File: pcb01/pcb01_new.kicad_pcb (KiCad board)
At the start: 2 copper layers, 116.8 x 91.4 mm, 51 parts, among them J1 DIN41612_02x32_AC, J10 Conn_01x02_Socket, J11 Conn_01x09, J5 UART, J7 Jmp_Irq, J8 Jmp_NMI, J9 Ram1 Enable, SW1 SW_Push, U1 W65C02SxP, U10 TL28L92FR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

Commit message: more routing
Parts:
- added J2: Jmp_UART_Irq, Connector_PinSocket_2.54mm:PinSocket_1x02_P2.54mm_Vertical, F.Cu at (137.2, 36.8)
- added J3: Conn_01x09_Socket, Connector_PinHeader_2.54mm:PinHeader_1x09_P2.54mm_Vertical, F.Cu at (135.9, 29.8)
- added J4: Conn_01x08_Socket, Connector_PinSocket_2.54mm:PinSocket_1x08_P2.54mm_Vertical, F.Cu at (135.9, 24.8)
- moved J5 1.27 mm to (137.2, 58.4)
- moved C1 0.67 mm to (123.3, 34.9)
- moved Y1 0.62 mm to (119.4, 39.4)
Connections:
- U10 pad 10: unconnected-(U10-OP7-Pad10) -> /UART_OP7
- U10 pad 18: unconnected-(U10-INTRN-Pad18) -> /~{IRQ_UART}
- U10 pad 2: unconnected-(U10-IP0-Pad2) -> /UART_IP0
- U10 pad 24: unconnected-(U10-OP6-Pad24) -> /UART_OP6
- U10 pad 25: unconnected-(U10-OP4-Pad25) -> /UART_OP4
- U10 pad 26: unconnected-(U10-OP2-Pad26) -> /UART_OP2
- U10 pad 27: unconnected-(U10-OP0-Pad27) -> /UART_OP0
- U10 pad 34: unconnected-(U10-IP2-Pad34) -> /UART_IP2
- U10 pad 35: unconnected-(U10-IP6-Pad35) -> /UART_IP6
- U10 pad 36: unconnected-(U10-IP5-Pad36) -> /UART_IP5
- U10 pad 37: unconnected-(U10-IP4-Pad37) -> /UART_IP4
- U10 pad 41: unconnected-(U10-IP3-Pad41) -> /UART_IP3
- U10 pad 43: unconnected-(U10-IP1-Pad43) -> /UART_IP1
- U10 pad 7: unconnected-(U10-OP1-Pad7) -> /UART_OP1
- U10 pad 8: unconnected-(U10-OP3-Pad8) -> /UART_OP3
- U10 pad 9: unconnected-(U10-OP5-Pad9) -> /UART_OP5
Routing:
- net GND: track 420.1 -> 570.4 mm, vias 32 -> 31
- net /UART_IP6: track 0.00 -> 57.8 mm
- net /UART_OP4: track 0.00 -> 52.7 mm
- net /UART_IP2: track 0.00 -> 52.0 mm, vias 0 -> 1
- net /UART_OP0: track 0.00 -> 46.9 mm, vias 0 -> 1
- net /UART_OP6: track 0.00 -> 44.2 mm
- net /UART_IP5: track 0.00 -> 43.4 mm
- net /UART_OP2: track 0.00 -> 40.8 mm, vias 0 -> 1
- net /UART_IP4: track 0.00 -> 39.5 mm, vias 0 -> 1
- net /UART_IP3: track 0.00 -> 33.2 mm, vias 0 -> 1
- net /UART_IP1: track 0.00 -> 27.6 mm, vias 0 -> 1
- net /~{IRQ_UART}: track 0.00 -> 27.0 mm, vias 0 -> 3
- net /UART_IP0: track 0.00 -> 22.1 mm, vias 0 -> 1
- net /UART_OP1: track 0.00 -> 18.7 mm, vias 0 -> 1
- net /UART_OP7: track 0.00 -> 18.2 mm
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
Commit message: finished mark2 pcb kind of
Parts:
- added R3: R, Resistor_THT:R_Axial_DIN0207_L6.3mm_D2.5mm_P7.62mm_Horizontal, F.Cu at (119.4, 20.3)
- U1: value W65C02SxP -> W65C02
- U2: value HM62256BLP -> Ram0
- U3: value 27C512 -> Rom
- U7: value HM62256BLP -> Ram1
- moved C13 80.4 mm to (124.5, 93.3)
- moved D1 7.62 mm to (129.8, 66.7)
- moved D4 7.62 mm to (129.8, 74.3)
- moved D5 7.62 mm to (129.8, 76.8)
- moved D8 7.62 mm to (129.8, 84.5)
- moved C11 5.08 mm to (30.5, 87.0), turned to 180 degrees
- moved D6 2.54 mm to (129.8, 79.4)
- moved D7 2.54 mm to (129.8, 81.9)
- moved D2 2.54 mm to (129.8, 69.2)
- moved D3 2.54 mm to (129.8, 71.8)
- moved RN1 1.16 mm to (131.4, 63.4)
- moved RN2 1.03 mm to (131.4, 87.7)
- renumbered SW1 to Reset
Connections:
- D1 pad 2: /GPIO00_O3 -> /GPIO00_O0
- D2 pad 2: /GPIO00_O2 -> /GPIO00_O1
- D3 pad 2: /GPIO00_O1 -> /GPIO00_O2
- D4 pad 2: /GPIO00_O0 -> /GPIO00_O3
- D5 pad 2: /GPIO00_O7 -> /GPIO00_O4
- D6 pad 2: /GPIO00_O6 -> /GPIO00_O5
- D7 pad 2: /GPIO00_O5 -> /GPIO00_O6
- D8 pad 2: /GPIO00_O4 -> /GPIO00_O7
- J2 pad 1: unconnected-(J2-Pin_1-Pad1) -> GND
- RN1 pad 1: Net-(D4-K) -> Net-(D1-K)
- RN1 pad 2: Net-(D3-K) -> Net-(D2-K)
- RN1 pad 3: Net-(D2-K) -> Net-(D3-K)
- RN1 pad 4: Net-(D1-K) -> Net-(D4-K)
- RN2 pad 1: Net-(D8-K) -> Net-(D5-K)
- RN2 pad 2: Net-(D7-K) -> Net-(D6-K)
- RN2 pad 3: Net-(D6-K) -> Net-(D7-K)
- RN2 pad 4: Net-(D5-K) -> Net-(D8-K)
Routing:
- net /D3: track 116.4 -> 148.6 mm
- net /~{IRQ_UART}: track 27.0 -> 59.0 mm, vias 3 -> 4
- net /D4: track 115.9 -> 142.0 mm, vias 4 -> 3
- net /D5: track 119.0 -> 139.5 mm
- net /D1: track 136.1 -> 154.1 mm, vias 7 -> 6
- net /D2: track 125.1 -> 140.6 mm, vias 5 -> 4
- net /D6: track 126.2 -> 137.8 mm
- net Net-(D1-K): track 12.2 -> 2.80 mm
- net Net-(D8-K): track 11.1 -> 3.05 mm
- net Net-(D5-K): track 3.23 -> 10.9 mm
- net Net-(D4-K): track 4.04 -> 11.1 mm
- net /D7: track 124.4 -> 130.4 mm
- net GND: track 570.4 -> 575.8 mm, vias 31 -> 46
- net /UART_IP6: track 57.8 -> 52.6 mm
- net VCC: track 523.2 -> 528.0 mm
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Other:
- board size 116.8 x 91.4 mm -> 119.4 x 91.4 mm
- board text added: "0"
- board text added: "32K"
- board text added: "64K"
- board text added: "IP"
- board text added: "Irq"
- board text added: "OP"
- board text added: "Rx1"
- board text added: "Rx2"
- board text added: "Tx1"
- board text added: "Tx2"
- board text added: "~{R0}"
- board text added: "~{RES}"
- board text added: "~{ROM}"
- board text added: "~{WE}"

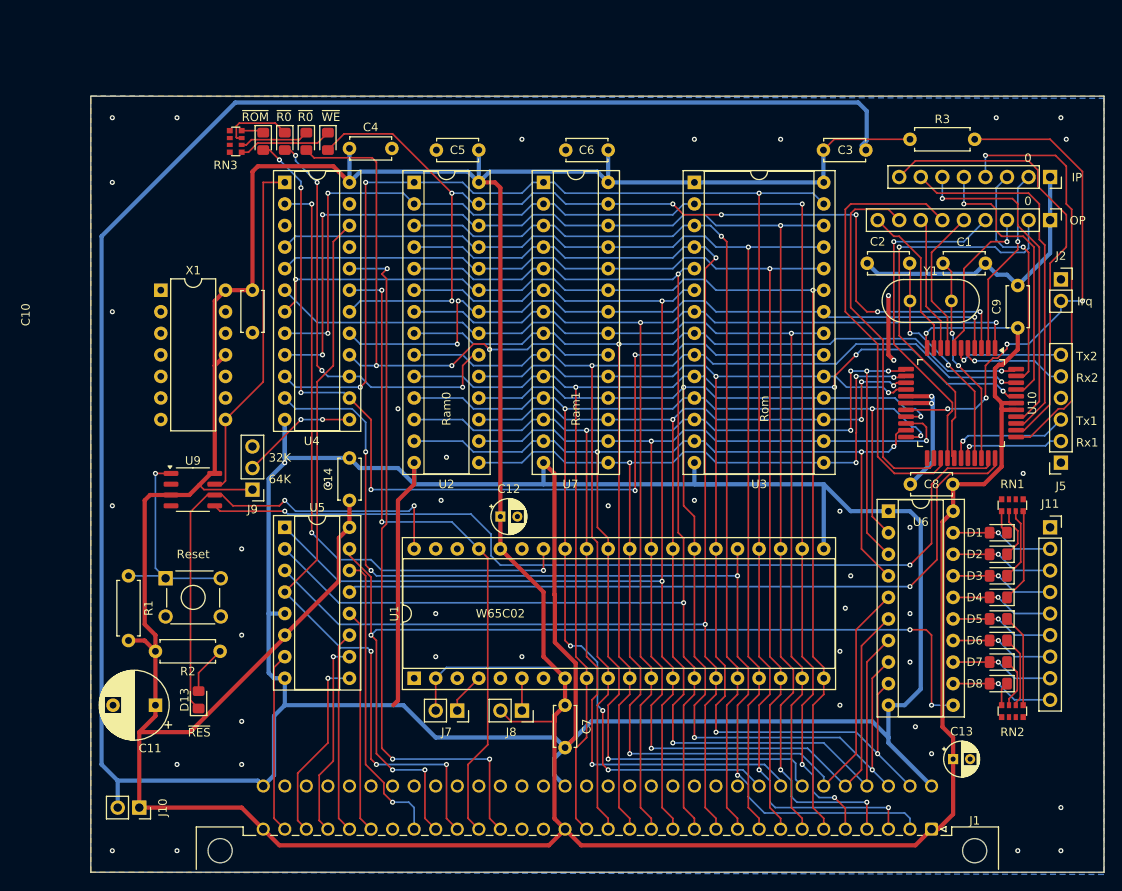
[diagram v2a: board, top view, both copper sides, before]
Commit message: add power switch etc
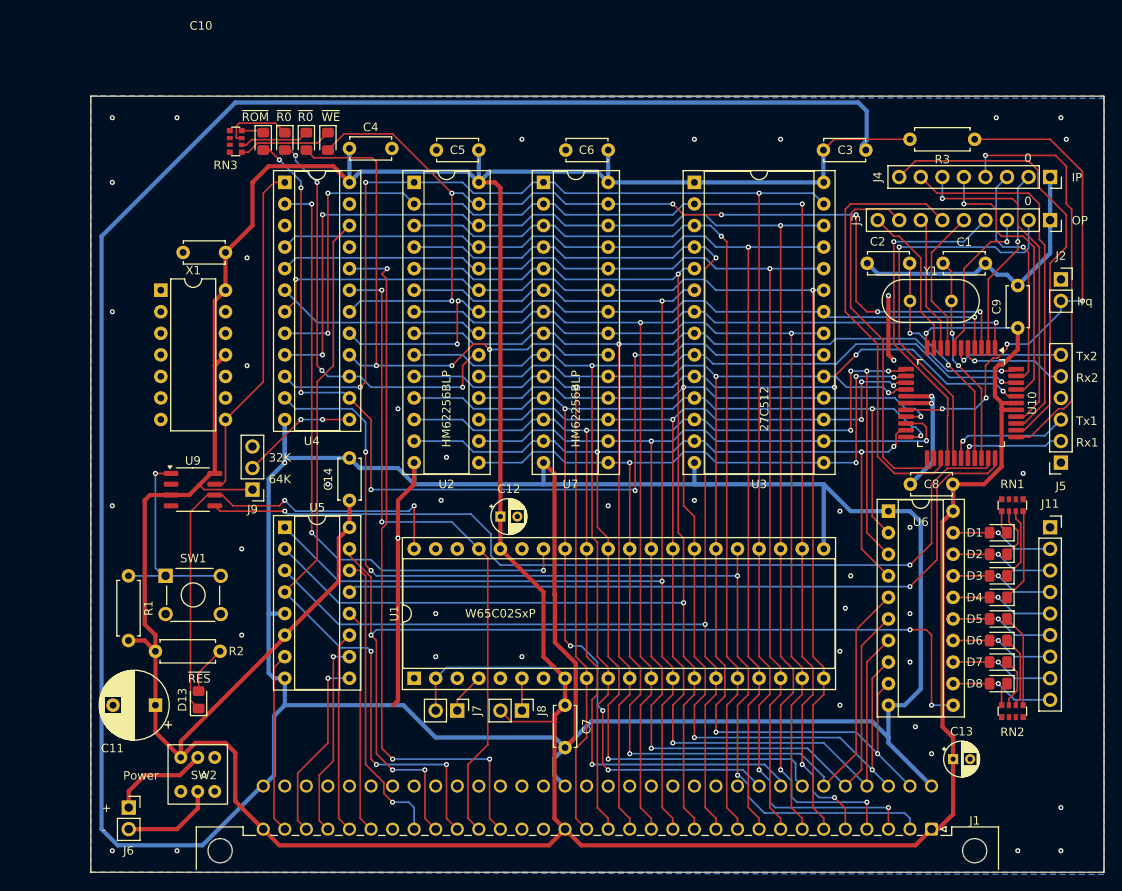
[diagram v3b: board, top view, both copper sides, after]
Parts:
- removed J10: Conn_01x02_Socket, Connector_PinSocket_2.54mm:PinSocket_1x02_P2.54mm_Vertical
- removed Reset: SW_Push, Button_Switch_THT:SW_TH_Tactile_Omron_B3F-10xx
- added J6: Conn_01x02_Socket, Connector_PinSocket_2.54mm:PinSocket_1x02_P2.54mm_Vertical, F.Cu at (27.3, 99.1)
- added SW1: SW_Push, Button_Switch_THT:SW_TH_Tactile_Omron_B3F-10xx, F.Cu at (31.7, 71.8)
- added SW2: SW_DPDT_x2, sim82:7x7DPDT, F.Cu at (37.5, 103.2)
- J3: footprint Connector_PinHeader_2.54mm:PinHeader_1x09_P2.54mm_Vertical -> Connector_PinSocket_2.54mm:PinSocket_1x09_P2.54mm_Vertical
- J7, J8: footprint Connector_PinSocket_2.54mm:PinSocket_1x02_P2.54mm_Vertical -> Connector_PinHeader_2.54mm:PinHeader_1x02_P2.54mm_Vertical
- U1: value W65C02 -> W65C02SxP
- U2: value Ram0 -> HM62256BLP
- U3: value Rom -> 27C512
- U7: value Ram1 -> HM62256BLP
- moved R3 7.62 mm to (127.0, 20.3), turned to 180 degrees
- moved C10 5.46 mm to (38.7, 33.7), turned to 180 degrees
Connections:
- R3 pad 1: VCC -> /~{IRQ_UART}
- R3 pad 2: /~{IRQ_UART} -> VCC
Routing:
- net Net-(J6-Pin_1): track 0.00 -> 11.7 mm
- net Net-(J6-Pin_2): track 0.00 -> 11.1 mm
- net VCC: track 528.0 -> 519.8 mm
- net GND: track 575.8 -> 582.9 mm, vias 46 -> 47
- net /CLOCK: track 41.0 -> 40.2 mm
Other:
- board text added: "+"
- board text added: "-"
- board text added: "Power"

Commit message: finalized (?) pcb
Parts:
- added H1: GND, MountingHole:MountingHole_3.2mm_M3_DIN965_Pad, F.Cu at (26.7, 19.1)
- added H2: GND, MountingHole:MountingHole_3.2mm_M3_DIN965_Pad, F.Cu at (138.4, 19.1)
- C3, C4: value C -> 100uF
- SW1: value SW_Push -> SW_Reset
- SW2: value SW_DPDT_x2 -> SW_PWR
- U2, U7: value HM62256BLP -> H3-65756H-5
- U4: value PAL20RS10 -> ATF22V10
- X1: value ACO-xxxMHz -> ACO-14MHz
- Y1: value Crystal -> Crystal 3.6864MHz
- moved SW2 8.19 mm to (35.5, 95.2)
- turned D10 to 90 degrees
- turned D11 to 90 degrees
- turned D12 to 90 degrees
- turned D9 to 90 degrees
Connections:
- D10 pad 1: Net-(D10-K) -> /~{CS_RAM0}
- D10 pad 2: /~{CS_RAM0} -> Net-(D10-A)
- D11 pad 1: Net-(D11-K) -> /~{CS_RAM1}
- D11 pad 2: /~{CS_RAM1} -> Net-(D11-A)
- D12 pad 1: Net-(D12-K) -> /~{QWE_RAM}
- D12 pad 2: /~{QWE_RAM} -> Net-(D12-A)
- D9 pad 1: Net-(D9-K) -> /~{CS_ROM}
- D9 pad 2: /~{CS_ROM} -> Net-(D9-A)
- J1 pad c30: unconnected-(J1-Pin_c30-Padc30) -> /RES
- J1 pad c31: unconnected-(J1-Pin_c31-Padc31) -> /~{RES}
- RN3 pad 1: Net-(D12-K) -> Net-(D12-A)
- RN3 pad 2: Net-(D11-K) -> Net-(D11-A)
- RN3 pad 3: Net-(D10-K) -> Net-(D10-A)
- RN3 pad 4: Net-(D9-K) -> Net-(D9-A)
- RN3 pad 5: GND -> VCC
- RN3 pad 6: GND -> VCC
- RN3 pad 7: GND -> VCC
- RN3 pad 8: GND -> VCC
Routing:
- net /RES: track 105.4 -> 145.8 mm, vias 2 -> 5
- net /~{RES}: track 57.4 -> 74.6 mm, vias 2 -> 4
- net Net-(D12-K): track 11.1 -> 0.00 mm
- net Net-(D12-A): track 0.00 -> 11.1 mm
- net VCC: track 519.8 -> 529.6 mm
- net Net-(D10-K): track 8.32 -> 0.00 mm
- net Net-(D10-A): track 0.00 -> 8.32 mm
- net Net-(D11-K): track 8.21 -> 0.00 mm
- net Net-(D11-A): track 0.00 -> 8.21 mm
- net Net-(D9-K): track 2.64 -> 0.00 mm
- net Net-(D9-A): track 0.00 -> 2.64 mm
- net GND: track 582.9 -> 584.5 mm, vias 47 -> 44
- net Net-(J6-Pin_2): track 11.1 -> 10.6 mm
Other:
- board text added: "6502 SBC Mark2"
- board text added: "NMI"
- board text added: "R0"
- board text added: "R1"
- board text added: "RES"
- board text added: "ROM"
- board text added: "Reset"
- board text added: "WE"
- board text removed: "~{R0}"
- board text removed: "~{RES}"
- board text removed: "~{ROM}"
- board text removed: "~{WE}"

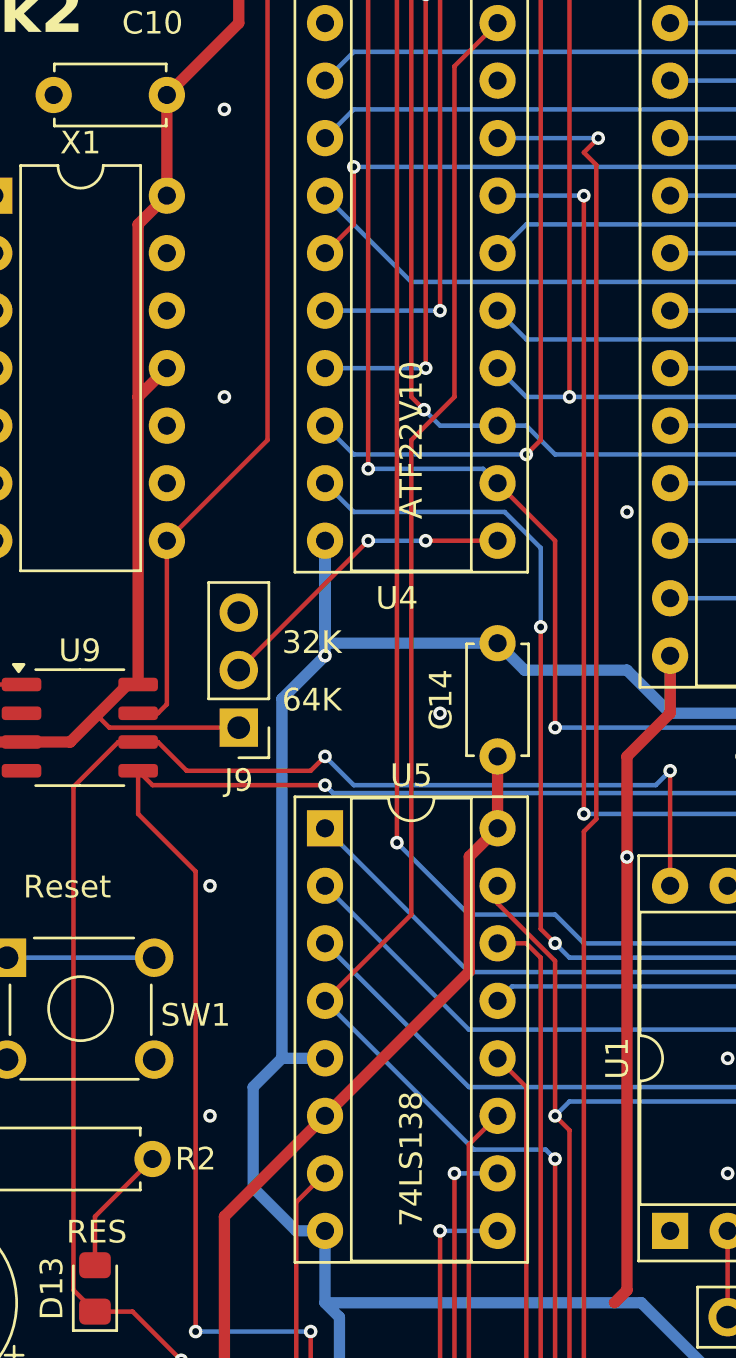
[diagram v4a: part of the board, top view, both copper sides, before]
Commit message: annotate values & add reset pull-up
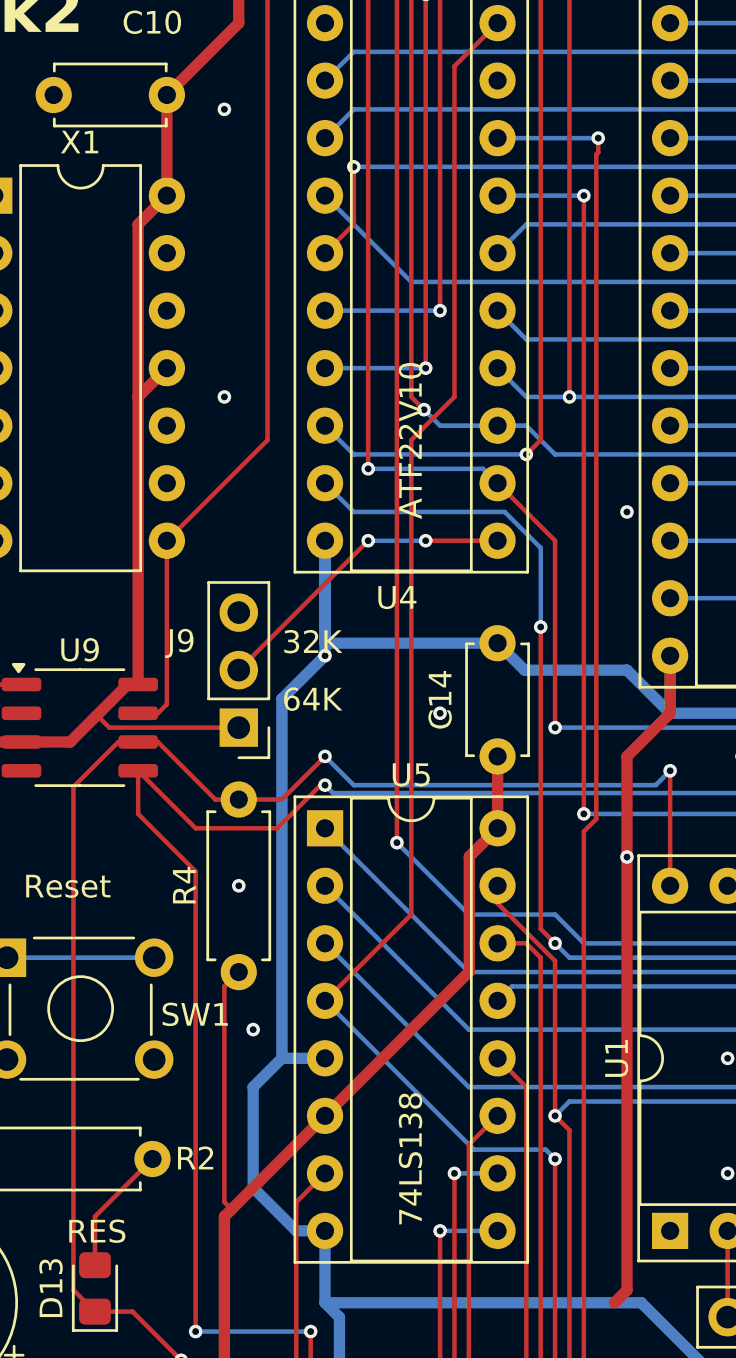
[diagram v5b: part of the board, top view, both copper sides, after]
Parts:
- added R4: 10K, Resistor_THT:R_Axial_DIN0207_L6.3mm_D2.5mm_P7.62mm_Horizontal, F.Cu at (41.9, 72.4)
- C1, C10, C14, C2, C5, C6, C7, C8, C9: value C -> 100nF
- C11: value C_Polarized -> 680uF
- C12, C13: value C_Polarized -> 47uF
- C3, C4: value 100uF -> 100nF
- R1, R2, R3: value R -> 10K
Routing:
- net VCC: track 529.6 -> 540.5 mm
- net /RES: track 145.8 -> 147.4 mm
- net /~{RES}: track 74.6 -> 75.7 mm
